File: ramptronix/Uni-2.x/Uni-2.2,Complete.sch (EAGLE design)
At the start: 115 parts, among them IC1 MCP14A0304T-E_SN, IC2 UCC38083DR, IC3 ME3116, IC4 ME3116, IC5 TL431CL3T, J1 TB005-762-02BE, J2 61300211121, Q1 STB130N6F7, Q2 STB130N6F7, T1 BIGTRANS, T1.1 B66362B1014T001

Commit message: Added Latest Board Revisions and Changelog.txt file
see title
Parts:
- removed C19: 100 pF, rcl:C-EUC0402K
- removed IC3: ME3116, SamacSys_Parts:ME3116
- removed INPUT: TB005-762-02BE, SamacSys_Parts:TB005-762-02BE
- removed U$4: HV, RMP - HALF BRIDGE 0.0.1:HV
- added C36: (no value), rcl:C-EUC1210K
- added IC7: ME3116, SamacSys_Parts:ME3116
- added J3: TB005-762-02BE, SamacSys_Parts:TB005-762-02BE
- added U$2: HV, RMP - HALF BRIDGE 0.0.1:HV
- C1, C13: value OVK151M1VTR-10131 -> 10 uF; device SamacSys_Parts:OVK151M1VTR-10131 -> rcl:C-EUC0603K; LCSC_PART (none) -> C440198
- C10: device rcl:C-EUC0805K -> rcl:C-EUC0603K
- C11: device rcl:C-EUC0805K -> rcl:C-EUC0603K; LCSC_PART C440198 -> (none)
- C12: value OVK151M1VTR-10131 -> 100 pF; device SamacSys_Parts:OVK151M1VTR-10131 -> rcl:C-EUC0402K; LCSC_PART (none) -> C1546
- C14: value 10 uF -> 470 pF; LCSC_PART C440198 -> C1620
- C15: value 0.1 uF -> 400BXW100MEFR18X25; device rcl:C-EUC0603K -> SamacSys_Parts:400BXW100MEFR18X25; LCSC_PART C440198 -> (none)
- C16: value 470 pF -> 400BXW100MEFR18X25; device rcl:C-EUC0603K -> SamacSys_Parts:400BXW100MEFR18X25; LCSC_PART C1620 -> (none)
- C17: value 2.2nF -> C1812C274KCRACAUTO; device rcl:C-EUC0603K -> SamacSys_Parts:C1812C274KCRACAUTO
- C18: value 470pF -> C1812C274KCRACAUTO; device rcl:C-EUC0603K -> SamacSys_Parts:C1812C274KCRACAUTO
- C2: value OVK151M1VTR-10131 -> 0.1 uF; device SamacSys_Parts:OVK151M1VTR-10131 -> rcl:C-EUC0603K; LCSC_PART (none) -> C440198
- C20: value 0.1 uF -> 470pF; LCSC_PART C14663 -> (none)
- C21: value 10 uF -> 2.2nF; device rcl:C-EUC0805K -> rcl:C-EUC0603K
- C22: device rcl:C-EUC0402 -> rcl:C-EUC0805K
- C23, C32: device rcl:C-EUC0603K -> rcl:C-EUC0805K
- C24: value 10 uF -> 1 uF
- C25: value 100 pF -> 10 uF; device rcl:C-EUC0402K -> rcl:C-EUC0603K; LCSC_PART C1546 -> C440198
- C26: value 1 uF -> 10 uF; device rcl:C-EUC0603K -> rcl:C-EUC0805K
- C3: value (none) -> OVK151M1VTR-10131; device rcl:C-EUC1210K -> SamacSys_Parts:OVK151M1VTR-10131
- C30: value 10 uF -> 100 pF; device rcl:C-EUC0805K -> rcl:C-EUC0402K; LCSC_PART C440198 -> C1546
- C31: device rcl:C-EUC0805K -> rcl:C-EUC0402
- C33: LCSC_PART (none) -> C440198
- C34: device rcl:C-EUC0805K -> rcl:C-EUC0603K; LCSC_PART (none) -> C440198
- C35: value 10 uF -> 1 uF; device rcl:C-EUC0603K -> rcl:C-EUC0805K
- C4, C5: value C1812C274KCRACAUTO -> OVK151M1VTR-10131; device SamacSys_Parts:C1812C274KCRACAUTO -> SamacSys_Parts:OVK151M1VTR-10131
- C6: value 400BXW100MEFR18X25 -> OVK151M1VTR-10131; device SamacSys_Parts:400BXW100MEFR18X25 -> SamacSys_Parts:OVK151M1VTR-10131
- C7: value 400BXW100MEFR18X25 -> 10 uF; device SamacSys_Parts:400BXW100MEFR18X25 -> rcl:C-EUC0805K
- C8: value 1 uF -> 0.1 uF; device rcl:C-EUC0805K -> rcl:C-EUC0603K; LCSC_PART C440198 -> C14663
- C9: device rcl:C-EUC0603K -> rcl:C-EUC0805K; LCSC_PART C440198 -> (none)
- GATE1_TP, GATE2_TP: value TPTP13R -> TPSQPAD1-17; device testpad:TPTP13R -> testpad:TPSQPAD1-17
- IC1: value MCP14A0304T-E_SN -> UCC38083DR; device SamacSys_Parts:MCP14A0304T-E_SN -> SamacSys_Parts:UCC38083DR
- IC2: value UCC38083DR -> MCP14A0304T-E_SN; device SamacSys_Parts:UCC38083DR -> SamacSys_Parts:MCP14A0304T-E_SN
- J1: value TB005-762-02BE -> 61300211121; device SamacSys_Parts:TB005-762-02BE -> Headers:61300211121
- J2: value 61300211121 -> TB005-762-02BE; device Headers:61300211121 -> SamacSys_Parts:TB005-762-02BE
- L1: value 2300LL-102-V-RC -> LQH5BPN6R8NT0L; device SamacSys_Parts:2300LL-102-V-RC -> SamacSys_Parts:LQH5BPN6R8NT0L
- L3: value LQH5BPN6R8NT0L -> 2300LL-102-V-RC; device SamacSys_Parts:LQH5BPN6R8NT0L -> SamacSys_Parts:2300LL-102-V-RC
- R1: value (none) -> 1k; device rcl:R-US_R1206 -> rcl:R-US_R0603; LCSC_PART (none) -> C22975
- R10: value 470 -> 100k; device rcl:R-US_R0603 -> rcl:R-US_R1206; LCSC_PART C22975 -> (none)
- R12: value 1k -> 22k; LCSC_PART C22975 -> C31850
- R13: value 22k -> 470k; LCSC_PART C31850 -> C25811
- R14: value 470k -> 100k; device rcl:R-US_R0603 -> rcl:R-US_R1206; LCSC_PART C25811 -> (none)
- R16: value 100 -> 2.2k; device rcl:R-US_R1206 -> rcl:R-US_R0805
- R17: value 100 -> 820; device rcl:R-US_R1206 -> rcl:R-US_R0603
- R18: value 10k -> 330; device rcl:R-US_R0402 -> rcl:R-US_R0805; LCSC_PART C25779 -> (none)
- R19: value 10k -> 20k; device rcl:R-US_R0402 -> rcl:R-US_R1206; LCSC_PART C25779 -> (none)
- R2: value 10 -> 1k; device rcl:R-US_R0805 -> rcl:R-US_R0402
- R20: value 100k -> 470; device rcl:R-US_R0402 -> rcl:R-US_R0603; LCSC_PART C25741 -> C22975; SPICEPREFIX R -> (none)
- R21: value 330 -> 4.7k; device rcl:R-US_R0805 -> rcl:R-US_R0603; LCSC_PART (none) -> C22975
- R22: value 2.2k -> 20k; device rcl:R-US_R0805 -> rcl:R-US_R1206
- R23: value 100k -> 100
- R24: value 100k -> 2k; device rcl:R-US_R1206 -> rcl:R-US_R0603; LCSC_PART (none) -> C22975
- R25: value 100k -> 10k; device rcl:R-US_R1206 -> rcl:R-US_R0402; LCSC_PART (none) -> C25779
- R26, R28: value 20k -> 100k; device rcl:R-US_R1206 -> rcl:R-US_R0402; LCSC_PART (none) -> C25741; SPICEPREFIX (none) -> R
- R27: value 20k -> 560; device rcl:R-US_R1206 -> rcl:R-US_R0402; LCSC_PART (none) -> C4177; SPICEPREFIX (none) -> R
- R29, R30: value 20k -> 10k; device rcl:R-US_R1206 -> rcl:R-US_R0402; LCSC_PART (none) -> C25779
- R31: value 560 -> 100; device rcl:R-US_R0402 -> rcl:R-US_R1206; LCSC_PART C4177 -> (none); SPICEPREFIX R -> (none)
- R32: value 10k -> 1k; device rcl:R-US_R0402 -> rcl:R-US_R0603; LCSC_PART C25779 -> C22975
- R33: value 100k -> (none); device rcl:R-US_R0402 -> rcl:R-US_R1206; LCSC_PART C25741 -> (none); SPICEPREFIX R -> (none)
- R34: value 2k -> 20k; device rcl:R-US_R0603 -> rcl:R-US_R1206; LCSC_PART C22975 -> (none)
- R35: value 820 -> 20k; device rcl:R-US_R0603 -> rcl:R-US_R1206
- R36: value 1k -> 20k; device rcl:R-US_R0603 -> rcl:R-US_R1206; LCSC_PART C22975 -> (none)
- R4: value 1k -> 10; device rcl:R-US_R0402 -> rcl:R-US_R0805
- R5, R6: value 0.05 -> 10; device rcl:R-US_R2512 -> rcl:R-US_R0805
- R7, R8: value 10 -> 0.05; device rcl:R-US_R0805 -> rcl:R-US_R2512
- R9: value 4.7k -> 100k; device rcl:R-US_R0603 -> rcl:R-US_R1206; LCSC_PART C22975 -> (none)
- renumbered IC5 to IC6, PS1 to PS2, SJ100 to SJ1, T1.1 to T1.2
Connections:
- net AUXB: now also C10.2, C12.1, C25.2, C31.2, R29.1; no longer C19.1, C22.2, C23.2, C24.2, R18.1
- net AUXD: now also C7.1, C9.1, IC4.IN, R23.2, R28.1, R31.2; no longer C21.1, C34.1, IC3.IN, R16.2, R17.2, R20.1
- net BRIDGEGND: now also R7.2, R8.2; no longer R5.2, R6.2
- net BS1: now also IC7.BS; no longer IC4.BS
- net BS2: now also C8.1, IC4.BS; no longer C20.1, IC3.BS
- net CS-IN: now also C14.1, IC1.CS; no longer C16.1, IC2.CS
- net DC+: now also C15.+, C16.+, C17.1, C18.1, J3.2, L3.2, R35.2, R9.1; no longer C4.1, C5.1, C6.+, C7.+, J1.2, L1.2, R25.1, R26.2
- net DRAIN1: now also R33.1; no longer R1.1, T1.2.5, T1.6
- net DRAIN2: now also C36.2; no longer C3.2, T1.2.9, T1.3
- net EN1: now also IC7.EN, R26.2; no longer IC4.EN, R33.2
- net EN2: now also IC4.EN, R28.2; no longer IC3.EN, R20.2
- net FB1: now also C30.2, IC7.FB, R25.1, R27.1; no longer C25.2, IC4.FB, R31.1, R32.1
- net FB2: now also C12.2, IC4.FB, R29.2, R30.1; no longer C19.2, IC3.FB, R18.2, R19.1
- net GNDA: now also C1.2, C13.2, C2.2, C22.1, C23.1, C24.2, C26.1, C3.-, C33.1, C35.2, C4.-, C5.-, C6.-, IC7.GND, J2.2, R12.2, R21.1, R24.1, R27.2, R7.1, R8.1; no longer C1.-, C10.1, C11.1, C12.-, C13.-, C15.2, C16.2, C2.-, C26.2, C30.1, C31.1, C8.2, C9.2, IC4.GND, INPUT.2, R14.2, R31.2, R34.1, R5.1, R6.1, R9.1
- net N$1: now also R10.1, R9.2; no longer R24.1, R25.2
- net N$10: now also R20.1, R21.2; no longer R10.1, R9.2
- net N$11: now also C33.2; no longer C32.2
- net N$12: now also R36.1; no longer R30.1
- net N$13: now also IC1.ISET, R12.1; no longer IC2.ISET, R13.1
- net N$14: now also R19.1, R36.2; no longer R29.1, R30.2
- net N$15: now also R10.2, R14.1; no longer R23.1, R24.2
- net N$16: now also R16.1, R18.2; no longer R21.2, R22.1
- net N$17: now also R19.2, R22.1; no longer R28.1, R29.2
- net N$18: now also C20.2; no longer C18.2
- net N$19: now also R17.2; no longer R35.2
- net N$2: now also IC1.OUTA, IC2.INA; no longer IC1.INA, IC2.OUTA
- net N$21: now also C21.2; no longer C17.2
- net N$22: now also R24.2; no longer R34.2
- net N$24: now also R22.2, R34.1; no longer R27.1, R28.2
- net N$26: now also R32.2; no longer R36.2
- net N$27: now also R23.1, R31.1; no longer R16.1, R17.1
- net N$28: now also R34.2, R35.1; no longer R26.1, R27.2
- net N$29: now also C36.1, R33.2; no longer C3.1, R1.2
- net N$3: now also C20.1, C21.1, J1.1, R14.2, R16.2; no longer C17.1, C18.1, J2.1, R22.2, R23.2
- net N$5: now also IC1.OUTB, IC2.INB; no longer IC1.INB, IC2.OUTB
- net N$6: now also IC2.ENA, IC2.ENB, R2.1; no longer IC1.ENA, IC1.ENB, R4.1
- net N$7: now also IC2.OUT1, R4.1; no longer IC1.OUT1, R2.1
- net N$8: now also IC2.OUT2, R5.1, R6.1; no longer IC1.OUT2, R7.1, R8.1
- net OPTO-EMITT: now also IC1.CTRL, R1.2; no longer IC2.CTRL, R12.2
- net PRE: now also C26.2, C30.1, L1.2, R25.2; no longer C25.1, C30.2, L3.2, R32.2
- net PWRGND: now also C10.1, C11.1, C15.-, C16.-, C17.2, C18.2, C25.1, C31.1, C34.1, C7.2, C9.2, D4.A1, D4.A2, IC4.GND, J1.2, J3.1, R18.1, R30.2, R32.1; no longer C21.2, C22.1, C23.1, C24.1, C33.1, C34.2, C35.1, C4.2, C5.2, C6.-, C7.-, D3.A1, D3.A2, IC3.GND, J1.1, J2.2, R19.2, R21.1, R36.1
- net Q1G: now also R4.2; no longer R2.2
- net Q2G: now also R5.2, R6.2; no longer R7.2, R8.2
- net RECT: now also D3.K, L3.1; no longer D4.K, L1.1
- net REG: now also C1.1, C13.1, C2.1, C22.2, C32.2, R1.1, R2.2, R20.2; no longer C10.2, C14.1, C15.1, C31.2, C9.1, R10.2, R12.1, R4.2
- net REG5V: now also C11.2, C34.2, R17.1; no longer C33.2, C35.2, R35.1
- net RT: now also IC1.RT, R13.1; no longer IC2.RT, R14.1
- net SWITCH1: now also IC7.SW, L1.1; no longer IC4.SW, L3.1
- net SWITCH2: now also C8.2, IC4.SW; no longer C20.2, IC3.SW
- net TRANS1: now also D3.A1, D3.A2, D4.K; no longer D1.K, D2.A1, D2.A2
- net TRANS2: now also D1.K, D2.A1, D2.A2; no longer D3.K, D4.A1, D4.A2
- net VCC28V: now also C23.2, C24.1, C3.+, C35.1, C4.+, C5.+, C6.+, IC7.IN, J2.1, R26.1; no longer C1.+, C11.2, C12.+, C13.+, C2.+, C26.1, C8.1, IC4.IN, INPUT.1, R33.1
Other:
- note removed: "BYV29B-500,118 MURB2060CT"
- note removed: "DIODES SELECTION"
- note removed: "FET Selection:"
- note removed: "YJB200G06B STB130N6F7"

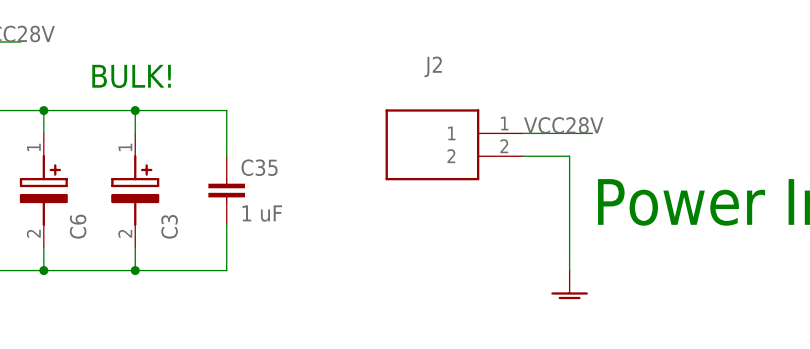
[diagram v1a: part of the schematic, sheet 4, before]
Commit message: Uni-2.2 HW Design Update EAGLE
Update
- Hole patterns
- LV Creapage/clearances
- PWR Plane stitching via locations
- PWR Plane routing
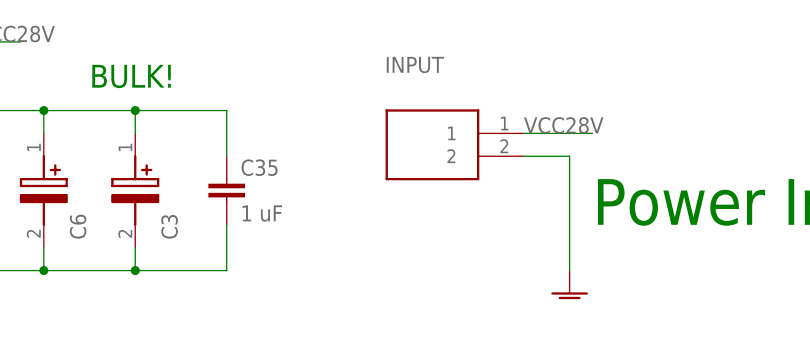
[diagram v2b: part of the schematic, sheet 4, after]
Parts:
- renumbered J2 to INPUT
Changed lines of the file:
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@@
 <drawing>
 <settings>
-<setting alwaysvectorfont="yes"/>
+<setting alwaysvectorfont="no"/>
 <setting verticaltext="up"/>
 </settings>
-<grid distance="0.1" unitdist="inch" unit="inch" style="dots" multiple="1" display="yes" altdistance="0.01" altunitdist="inch" altunit="inch"/>
+<grid distance="0.1" unitdist="inch" unit="inch" style="lines" multiple="1" display="no" altdistance="0.01" altunitdist="inch" altunit="inch"/>
 <layers>
-<layer number="1" name="Top" color="4" fill="1" visible="yes" active="no"/>
-<layer number="2" name="Route2" color="16" fill="1" visible="yes" active="no"/>
-<layer number="3" name="Route3" color="17" fill="1" visible="yes" active="no"/>
-<layer number="4" name="Route4" color="18" fill="1" visible="yes" active="no"/>
-<layer number="5" name="Route5" color="19" fill="1" visible="yes" active="no"/>
-<layer number="6" name="Route6" color="25" fill="1" visible="yes" active="no"/>
-<layer number="7" name="Route7" color="26" fill="1" visible="yes" active="no"/>
-<layer number="8" name="Route8" color="27" fill="1" visible="yes" active="no"/>
-<layer number="9" name="Route9" color="28" fill="1" visible="yes" active="no"/>
-<layer number="10" name="Route10" color="29" fill="1" visible="yes" active="no"/>
-<layer number="11" name="Route11" color="30" fill="1" visible="yes" active="no"/>
-<layer number="12" name="Route12" color="20" fill="1" visible="yes" active="no"/>
-<layer number="13" name="Route13" color="21" fill="1" visible="yes" active="no"/>
-<layer number="14" name="Route14" color="22" fill="1" visible="yes" active="no"/>
-<layer number="15" name="Route15" color="23" fill="1" visible="yes" active="no"/>
-<layer number="16" name="Bottom" color="1" fill="1" visible="yes" active="no"/>
-<layer number="17" name="Pads" color="2" fill="1" visible="yes" active="no"/>
-<layer number="18" name="Vias" color="2" fill="1" visible="yes" active="no"/>
-<layer number="19" name="Unrouted" color="6" fill="1" visible="yes" active="no"/>
-<layer number="20" name="Dimension" color="24" fill="1" visible="yes" active="no"/>
-<layer number="21" name="tPlace" color="7" fill="1" visible="yes" active="no"/>
-<layer number="22" name="bPlace" color="7" fill="1" visible="yes" active="no"/>
-<layer number="23" name="tOrigins" color="15" fill="1" visible="yes" active="no"/>
-<layer number="24" name="bOrigins" color="15" fill="1" visible="yes" active="no"/>
-<layer number="25" name="tNames" color="7" fill="1" visible="yes" active="no"/>
-<layer number="26" name="bNames" color="7" fill="1" visible="yes" active="no"/>
-<layer number="27" name="tValues" color="7" fill="1" visible="yes" active="no"/>
-<layer number="28" name="bValues" color="7" fill="1" visible="yes" active="no"/>
+<layer number="1" name="Top" color="4" fill="1" visible="no" active="no"/>
+<layer number="2" name="Route2" color="16" fill="1" visible="no" active="no"/>
+<layer number="3" name="Route3" color="17" fill="1" visible="no" active="no"/>
+<layer number="4" name="Route4" color="18" fill="1" visible="no" active="no"/>
+<layer number="5" name="Route5" color="19" fill="1" visible="no" active="no"/>
+<layer number="6" name="Route6" color="25" fill="1" visible="no" active="no"/>
+<layer number="7" name="Route7" color="26" fill="1" visible="no" active="no"/>
+<layer number="8" name="Route8" color="27" fill="1" visible="no" active="no"/>
+<layer number="9" name="Route9" color="28" fill="1" visible="no" active="no"/>
+<layer number="10" name="Route10" color="29" fill="1" visible="no" active="no"/>
+<layer number="11" name="Route11" color="30" fill="1" visible="no" active="no"/>
+<layer number="12" name="Route12" color="20" fill="1" visible="no" active="no"/>
+<layer number="13" name="Route13" color="21" fill="1" visible="no" active="no"/>
+<layer number="14" name="Route14" color="22" fill="1" visible="no" active="no"/>
+<layer number="15" name="Route15" color="23" fill="1" visible="no" active="no"/>
+<layer number="16" name="Bottom" color="1" fill="1" visible="no" active="no"/>
+<layer number="17" name="Pads" color="2" fill="1" visible="no" active="no"/>
+<layer number="18" name="Vias" color="2" fill="1" visible="no" active="no"/>
+<layer number="19" name="Unrouted" color="6" fill="1" visible="no" active="no"/>
+<layer number="20" name="Dimension" color="24" fill="1" visible="no" active="no"/>
+<layer number="21" name="tPlace" color="7" fill="1" visible="no" active="no"/>
+<layer number="22" name="bPlace" color="7" fill="1" visible="no" active="no"/>
+<layer number="23" name="tOrigins" color="15" fill="1" visible="no" active="no"/>
+<layer number="24" name="bOrigins" color="15" fill="1" visible="no" active="no"/>
+<layer number="25" name="tNames" color="7" fill="1" visible="no" active="no"/>
+<layer number="26" name="bNames" color="7" fill="1" visible="no" active="no"/>
+<layer number="27" name="tValues" color="7" fill="1" visible="no" active="no"/>
+<layer number="28" name="bValues" color="7" fill="1" visible="no" active="no"/>
 <layer number="29" name="tStop" color="7" fill="3" visible="no" active="no"/>
 <layer number="30" name="bStop" color="7" fill="6" visible="no" active="no"/>
@@
 <layer number="35" name="tGlue" color="7" fill="4" visible="no" active="no"/>
 <layer number="36" name="bGlue" color="7" fill="5" visible="no" active="no"/>
-<layer number="37" name="tTest" color="7" fill="1" visible="yes" active="no"/>
-<layer number="38" name="bTest" color="7" fill="1" visible="yes" active="no"/>
+<layer number="37" name="tTest" color="7" fill="1" visible="no" active="no"/>
+<layer number="38" name="bTest" color="7" fill="1" visible="no" active="no"/>
 <layer number="39" name="tKeepout" color="4" fill="11" visible="no" active="no"/>
 <layer number="40" name="bKeepout" color="1" fill="11" visible="no" active="no"/>
@@
 <layer number="44" name="Drills" color="7" fill="1" visible="no" active="no"/>
 <layer number="45" name="Holes" color="7" fill="1" visible="no" active="no"/>
-<layer number="46" name="Milling" color="3" fill="1" visible="yes" active="no"/>
-<layer number="47" name="Measures" color="7" fill="1" visible="yes" active="no"/>
-<layer number="48" name="Document" color="7" fill="1" visible="yes" active="no"/>
-<layer number="49" name="Reference" color="7" fill="1" visible="yes" active="no"/>
-<layer number="50" name="dxf" color="7" fill="1" visible="yes" active="no"/>
-<layer number="51" name="tDocu" color="7" fill="1" visible="yes" active="no"/>
-<layer number="52" name="bDocu" color="7" fill="1" visible="yes" active="no"/>
-<layer number="53" name="tGND_GNDA" color="7" fill="9" visible="yes" active="no"/>
-<layer number="54" name="bGND_GNDA" color="1" fill="9" visible="yes" active="no"/>
-<layer number="56" name="wert" color="7" fill="1" visible="yes" active="no"/>
-<layer number="57" name="tCAD" color="7" fill="1" visible="yes" active="no"/>
-<layer number="58" name="b3D" color="7" fill="1" visible="yes" active="no"/>
-<layer number="59" name="tCarbon" color="7" fill="1" visible="yes" active="no"/>
-<layer number="60" name="bCarbon" color="7" fill="1" visible="yes" active="no"/>
-<layer number="61" name="stand" color="7" fill="1" visible="yes" active="no"/>
+<layer number="46" name="Milling" color="3" fill="1" visible="no" active="no"/>
+<layer number="47" name="Measures" color="7" fill="1" visible="no" active="no"/>
+<layer number="48" name="Document" color="7" fill="1" visible="no" active="no"/>
+<layer number="49" name="Reference" color="7" fill="1" visible="no" active="no"/>
+<layer number="50" name="dxf" color="7" fill="1" visible="no" active="no"/>
+<layer number="51" name="tDocu" color="7" fill="1" visible="no" active="no"/>
+<layer number="52" name="bDocu" color="7" fill="1" visible="no" active="no"/>
+<layer number="53" name="tGND_GNDA" color="7" fill="9" visible="no" active="no"/>
+<layer number="54" name="bGND_GNDA" color="1" fill="9" visible="no" active="no"/>
+<layer number="56" name="wert" color="7" fill="1" visible="no" active="no"/>
+<layer number="57" name="tCAD" color="7" fill="1" visible="no" active="no"/>
+<layer number="58" name="b3D" color="7" fill="1" visible="no" active="no"/>
+<layer number="59" name="tCarbon" color="7" fill="1" visible="no" active="no"/>
+<layer number="60" name="bCarbon" color="7" fill="1" visible="no" active="no"/>
+<layer number="61" name="stand" color="7" fill="1" visible="no" active="no"/>
 <layer number="88" name="SimResults" color="9" fill="1" visible="yes" active="yes"/>
 <layer number="89" name="SimProbes" color="9" fill="1" visible="yes" active="yes"/>
@@
 </part>
 <part name="HVLED" library="led" library_urn="urn:adsk.eagle:library:259" deviceset="LED" device="CHIPLED_0805" package3d_urn="urn:adsk.eagle:package:15821/2" value="RED"/>
-<part name="J2" library="SamacSys_Parts" deviceset="TB005-762-02BE" device=""/>
+<part name="INPUT" library="SamacSys_Parts" deviceset="TB005-762-02BE" device=""/>
 <part name="J3" library="SamacSys_Parts" deviceset="TB005-762-02BE" device=""/>
 <part name="U$2" library="RMP - HALF BRIDGE 0.0.1" deviceset="HV" device=""/>
@@
 </instance>
 <instance part="GND7" gate="1" x="124.46" y="137.16" smashed="yes"/>
-<instance part="J2" gate="G$1" x="119.38" y="154.94" smashed="yes" rot="MR0">
+<instance part="INPUT" gate="G$1" x="119.38" y="154.94" smashed="yes" rot="MR0">
 <attribute name="NAME" x="110.49" y="162.56" size="1.778" layer="95" rot="MR0" align="center-left"/>
 </instance>
@@
 <pinref part="GND7" gate="1" pin="GNDA"/>
 <wire x1="124.46" y1="139.7" x2="124.46" y2="152.4" width="0.1524" layer="91"/>
-<pinref part="J2" gate="G$1" pin="2"/>
+<pinref part="INPUT" gate="G$1" pin="2"/>
 <wire x1="124.46" y1="152.4" x2="119.38" y2="152.4" width="0.1524" layer="91"/>
 </segment>
@@
 <net name="VCC28V" class="0">
 <segment>
-<pinref part="J2" gate="G$1" pin="1"/>
+<pinref part="INPUT" gate="G$1" pin="1"/>
 <wire x1="119.38" y1="154.94" x2="127" y2="154.94" width="0.1524" layer="91"/>
 <label x="119.38" y="154.94" size="1.778" layer="95"/>
